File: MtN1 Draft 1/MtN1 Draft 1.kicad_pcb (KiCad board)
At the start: 4 copper layers, 40 x 46 mm, 74 parts, among them J1 Motor_Port_1, J10 ServoPorts_2x3, J11 QWIIC, J12 PQWIIC, J13 GPIO_R1, J14 GPIO_R2, J15 GPIO_R3, J2 Motor_Port_2, J3 Motor_Port_3, J4 Motor_Port_4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

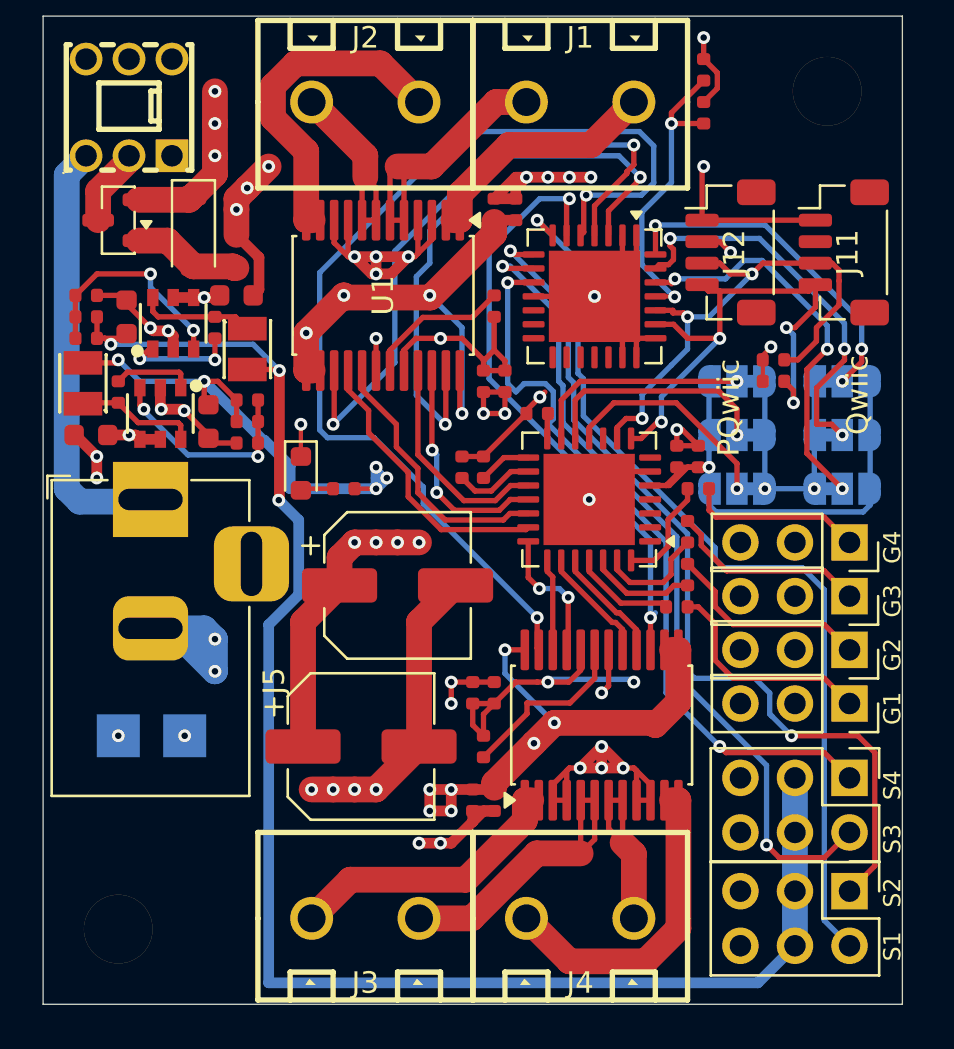
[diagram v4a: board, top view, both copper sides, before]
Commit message: Trace cleanup; extra labels
DRC likes me now 🎉, but probably not someone who understands electronics 😭
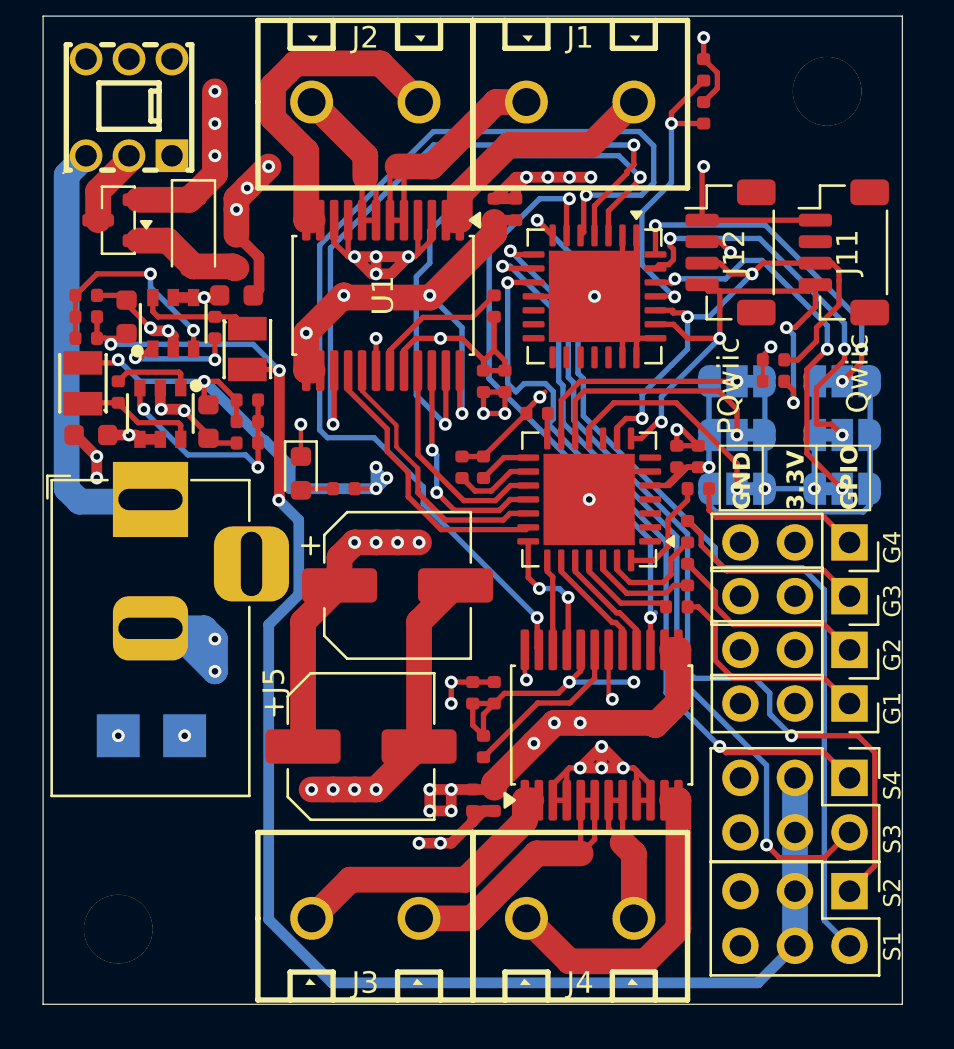
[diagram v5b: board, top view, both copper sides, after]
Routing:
- net VCC: track 73.2 -> 69.4 mm, vias 21 -> 22
- net MD1 PWMB: track 29.9 -> 31.9 mm
- net +5V: track 75.6 -> 73.9 mm
- net +3V3: track 95.8 -> 94.9 mm
- net MD2 PWMA: track 48.7 -> 49.4 mm
- net Net-(U7-FB): track 10.0 -> 10.8 mm
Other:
- board text added: "3.3V"
- board text added: "GPIO"

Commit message: Added Note To Silkscreen
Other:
- board text added: "In Memory of Buster <3"
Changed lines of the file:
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@@
+		)
+	)
+	(gr_text "In Memory of Buster <3"
+		(at 102 120.5 90)
+		(layer "B.SilkS")
+		(effects
+			(font
+				(size 1 1)
+				(thickness 0.1)
+			)
+			(justify left bottom mirror)
 		)
 	)
